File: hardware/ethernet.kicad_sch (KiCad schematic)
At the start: 92 parts, among them J5 USB_C_Receptacle, Q1 BSS138, Q2 BSS138, U11 TXS0202YZPR, U14 KSZ9031RNXCA, U4 CCGM1A1, X1 ECS-2520MV-250-xx

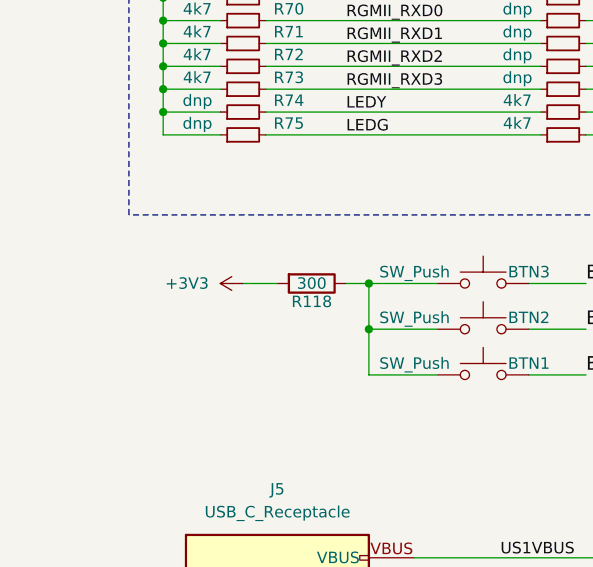
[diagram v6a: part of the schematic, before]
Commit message: Fixing button voltage - fix #6
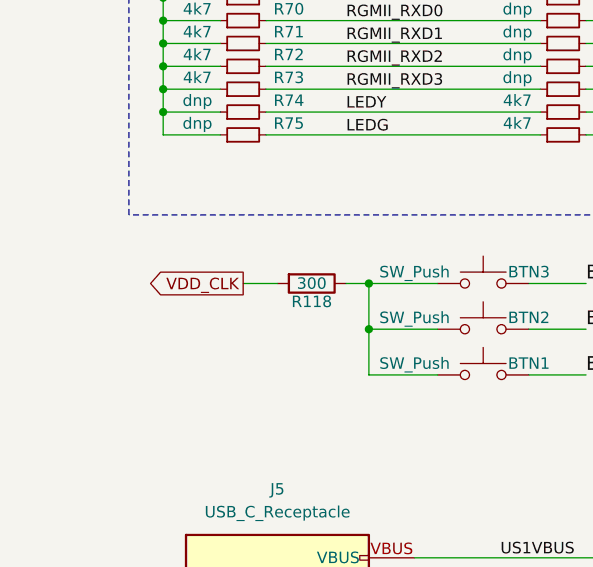
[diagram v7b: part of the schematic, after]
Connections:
- net +3V3: no longer R118.2
- net VDD_CLK: now also R118.2
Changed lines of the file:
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@@
+	(global_label "VDD_CLK"
+		(shape output)
+		(at 36.83 151.13 180)
+		(fields_autoplaced yes)
+		(effects
+			(font
+				(size 1.27 1.27)
+			)
+			(justify right)
+		)
+		(property "Intersheetrefs" "${INTERSHEET_REFS}"
+			(at 25.6805 151.13 0)
+			(effects
+				(font
+					(size 1.27 1.27)
+				)
+				(justify right)
+				(hide yes)
+			)
+		)
+	)
 	(global_label "VDD_CLK"
 		(shape output)
@@
 					(unit 1)
 				)
-			)
-		)
-	)
-	(symbol
-		(lib_name "+5V_1")
-		(lib_id "power:+5V")
-		(at 36.83 151.13 90)
-		(unit 1)
-		(exclude_from_sim no)
-		(in_bom yes)
-		(on_board yes)
-		(dnp no)
-		(fields_autoplaced yes)
-		(property "Reference" "#PWR0159"
-			(at 40.64 151.13 0)
-			(effects
-				(font
-					(size 1.27 1.27)
-				)
-				(hide yes)
-			)
-		)
-		(property "Value" "+3V3"
-			(at 33.02 151.1299 90)
-			(effects
-				(font
-					(size 1.27 1.27)
-				)
-				(justify left)
-			)
-		)
-		(property "Footprint" ""
-			(at 36.83 151.13 0)
-			(effects
-				(font
-					(size 1.27 1.27)
-				)
-				(hide yes)
-			)
-		)
-		(property "Datasheet" ""
-			(at 36.83 151.13 0)
-			(effects
-				(font
-					(size 1.27 1.27)
-				)
-				(hide yes)
-			)
-		)
-		(property "Description" "Power symbol creates a global label with name \"+5V\""
-			(at 36.83 151.13 0)
-			(effects
-				(font
-					(size 1.27 1.27)
-				)
-				(hide yes)
-			)
-		)
-		(pin "1"
-		)
-		(instances
-			(project "ulx5m-gs"
-				(path "/9e5cbfd6-8186-4817-919e-acd256336bc8/5c4580e2-a442-496c-941e-38ded55dcc84"
-					(reference "#PWR0159")
-					(unit 1)
-				)

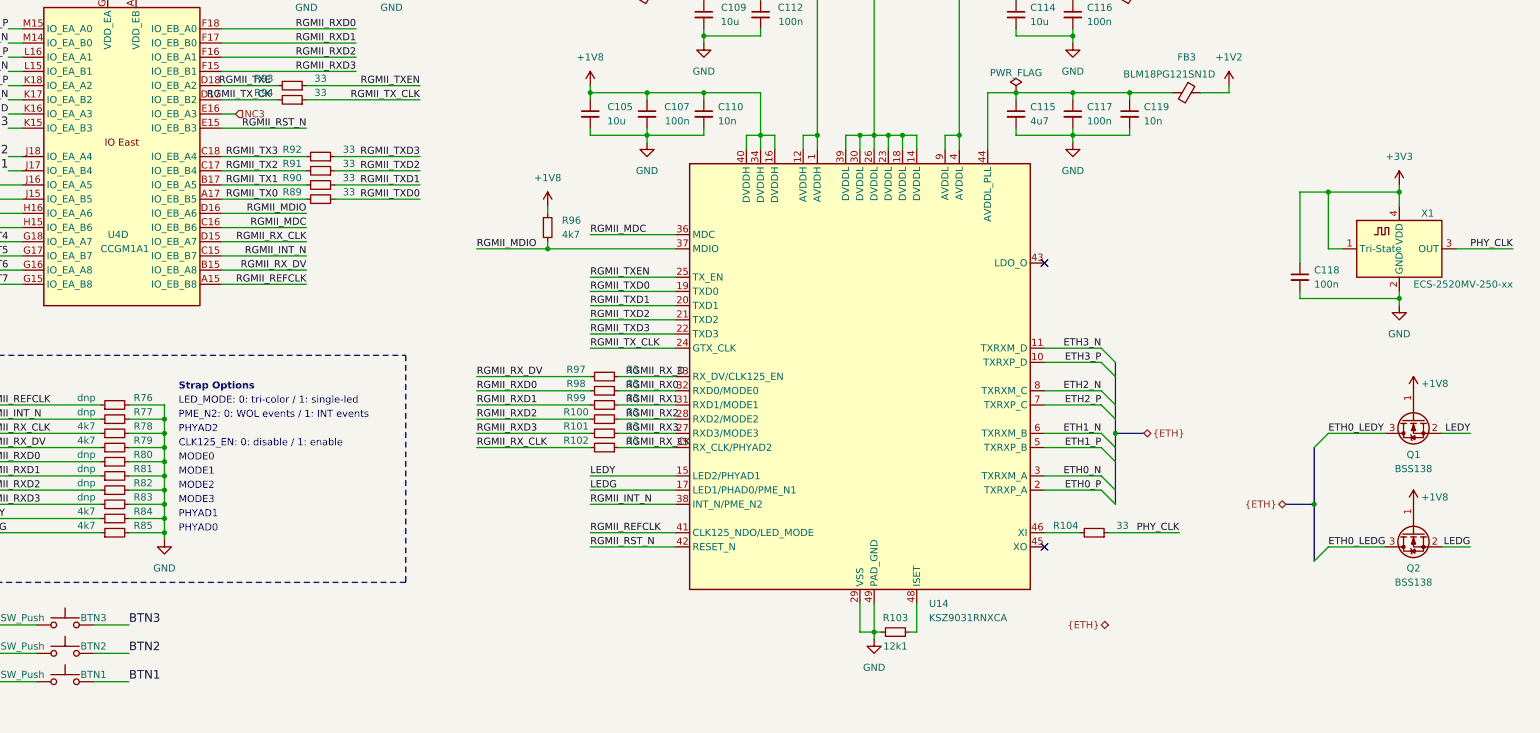
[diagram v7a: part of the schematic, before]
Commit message: Connecting PWR and FAN_PWM to NC pins, using NC3 for Ethernet clock
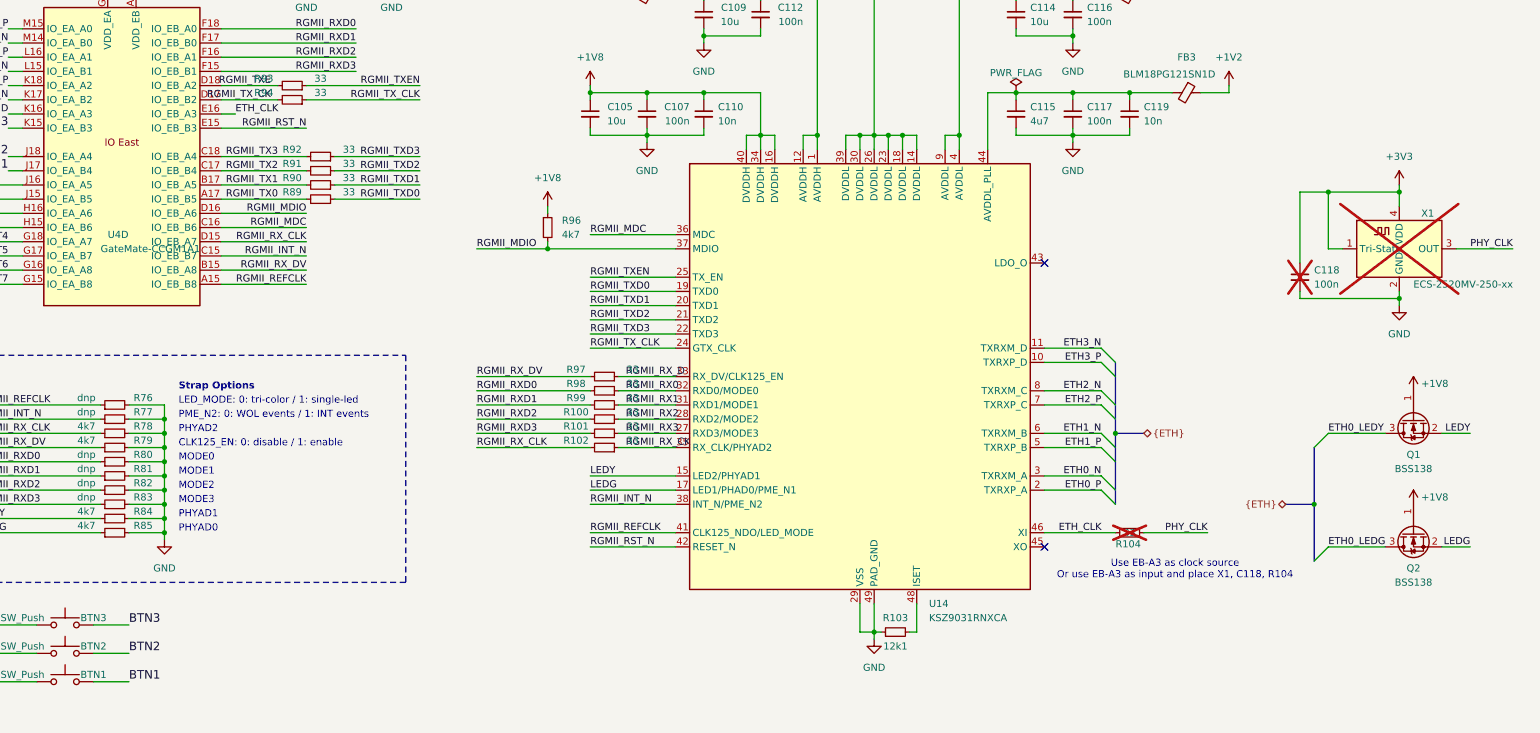
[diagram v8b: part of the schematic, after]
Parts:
- C118, R104, X1: now not fitted
- Q1, Q2: footprint Package_TO_SOT_SMD:SOT-23 -> Package_TO_SOT_SMD:SOT-523
- U4: value CCGM1A1 -> GateMate-CCGM1A1
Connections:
- net NC3 is gone; now on net ETH_CLK: U4.E16 (IO_EB_A3)
- net ETH_CLK: now reaches R104.2, U14.46 (XI)
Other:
- note added: "Use EB-A3 as clock source Or use EB-A3 as input and place X1, C118, R104"
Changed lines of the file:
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@@
 		)
 	)
+	(text "Use EB-A3 as clock source\nOr use EB-A3 as input and place X1, C118, R104"
+		(exclude_from_sim no)
+		(at 262.128 141.224 0)
+		(effects
+			(font
+				(size 1.27 1.27)
+			)
+		)
+	)
 	(text "D5,D7: Schottky 2A/30V \nLow drop Vfmax=0.375V\nParts reduction: Only D5 is required."
 		(exclude_from_sim no)
@@
 	(wire
 		(pts
-			(xy 250.19 134.62) (xy 262.89 134.62)
+			(xy 256.54 134.62) (xy 267.97 134.62)
 		)
 		(stroke
@@
 	(wire
 		(pts
-			(xy 238.76 134.62) (xy 245.11 134.62)
+			(xy 238.76 134.62) (xy 251.46 134.62)
 		)
 		(stroke
@@
 		)
 	)
+	(label "ETH_CLK"
+		(at 93.98 59.69 0)
+		(effects
+			(font
+				(size 1.27 1.27)
+			)
+			(justify left bottom)
+		)
+	)
 	(label "LEDG"
 		(at 314.96 137.16 180)
@@
 	)
 	(label "PHY_CLK"
-		(at 262.89 134.62 180)
+		(at 267.97 134.62 180)
 		(effects
 			(font
@@
 		)
 	)
+	(label "ETH_CLK"
+		(at 241.3 134.62 0)
+		(effects
+			(font
+				(size 1.27 1.27)
+			)
+			(justify left bottom)
+		)
+	)
 	(label "RGMII_MDC"
 		(at 106.68 80.01 180)
@@
 		)
 	)
-	(hierarchical_label "NC3"
-		(shape input)
-		(at 93.98 59.69 0)
-		(effects
-			(font
-				(size 1.27 1.27)
-			)
-			(justify left)
-		)
-	)
-	(hierarchical_label "{ETH}"
-		(shape bidirectional)
-		(at 250.19 151.13 180)
-		(effects
-			(font
-				(size 1.27 1.27)
-			)
-			(justify right)
-		)
-	)
 	(hierarchical_label "{ETH}"
 		(shape bidirectional)
@@
 			)
 		)
-		(property "Value" "CCGM1A1"
+		(property "Value" "GateMate-CCGM1A1"
 			(at 69.85 83.82 0)
 			(effects
@@
 			)
 		)
-		(property "Footprint" "Package_TO_SOT_SMD:SOT-23"
+		(property "Footprint" "Package_TO_SOT_SMD:SOT-523"
 			(at 306.705 119.38 0)
 			(effects
@@
 		(in_bom yes)
 		(on_board yes)
-		(dnp no)
+		(dnp yes)
 		(property "Reference" "X1"
 			(at 307.34 77.47 0)
@@
 	(symbol
 		(lib_id "Device:R_Small")
-		(at 247.65 134.62 270)
+		(at 254 134.62 270)
 		(mirror x)
 		(unit 1)
@@
 		(in_bom yes)
 		(on_board yes)
-		(dnp no)
+		(dnp yes)
 		(property "Reference" "R104"
-			(at 242.57 133.35 90)
+			(at 253.746 136.652 90)
 			(effects
 				(font
@@
 		)
 		(property "Value" "33"
-			(at 252.73 133.35 90)
+			(at 254 134.62 90)
 			(effects
 				(font
@@
 		)
 		(property "Footprint" "Resistor_SMD:R_0402_1005Metric"
-			(at 247.65 134.62 0)
+			(at 254 134.62 0)
 			(effects
 				(font
@@
 		)
 		(property "Datasheet" "~"
-			(at 247.65 134.62 0)
+			(at 254 134.62 0)
 			(effects
 				(font
@@
 		)
 		(property "Description" "Resistor, small symbol"
-			(at 247.65 134.62 0)
+			(at 254 134.62 0)
 			(effects
 				(font
@@
 			)
 		)
-		(property "Footprint" "Package_TO_SOT_SMD:SOT-23"
+		(property "Footprint" "Package_TO_SOT_SMD:SOT-523"
 			(at 306.705 139.7 0)
 			(effects
@@
 		(in_bom yes)
 		(on_board yes)
-		(dnp no)
+		(dnp yes)
 		(fields_autoplaced yes)
 		(property "Reference" "C118"
